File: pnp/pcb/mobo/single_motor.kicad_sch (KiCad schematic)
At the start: 8 parts, among them M2 Stepper_Motor

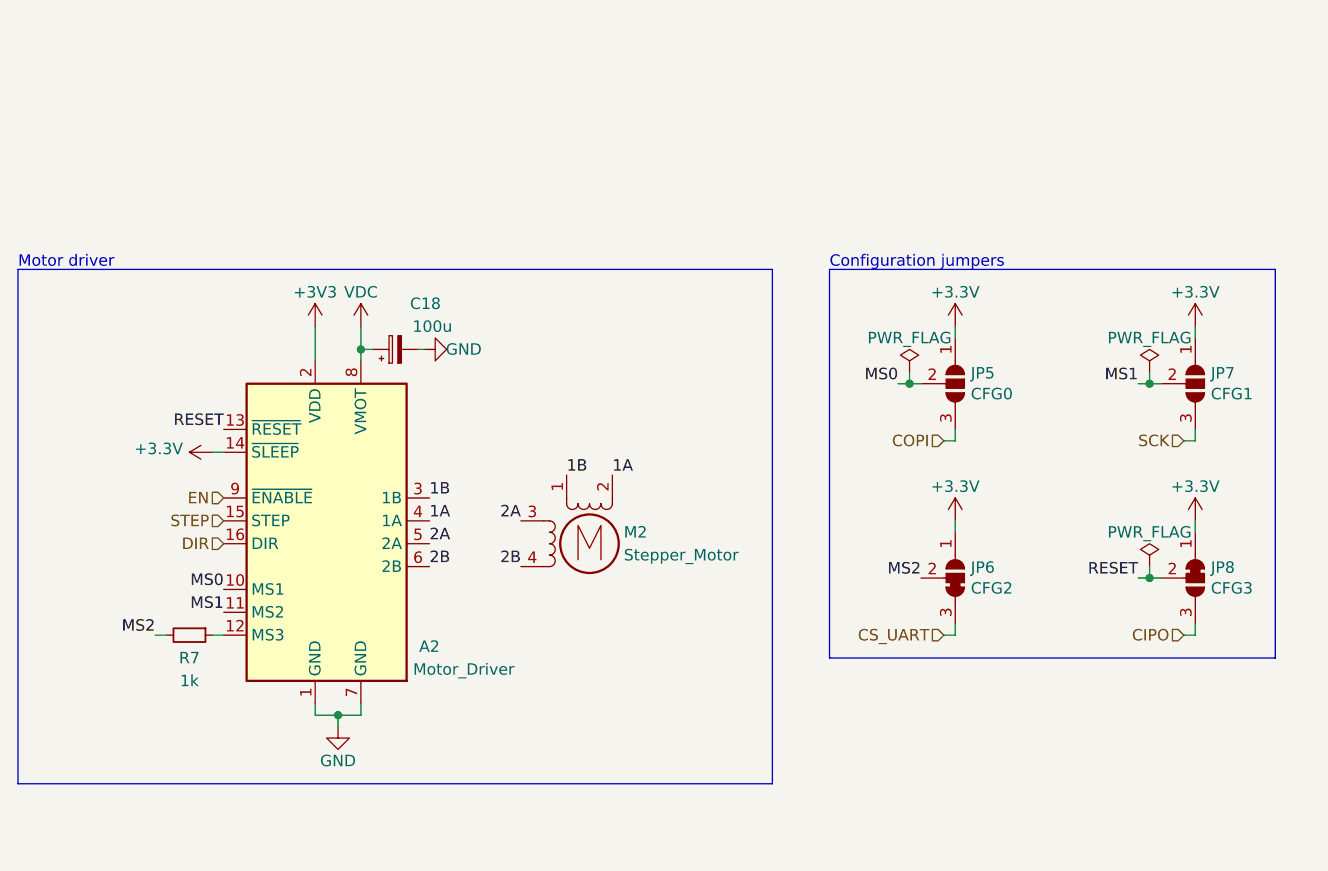
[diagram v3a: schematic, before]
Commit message: Fixed schematic parity
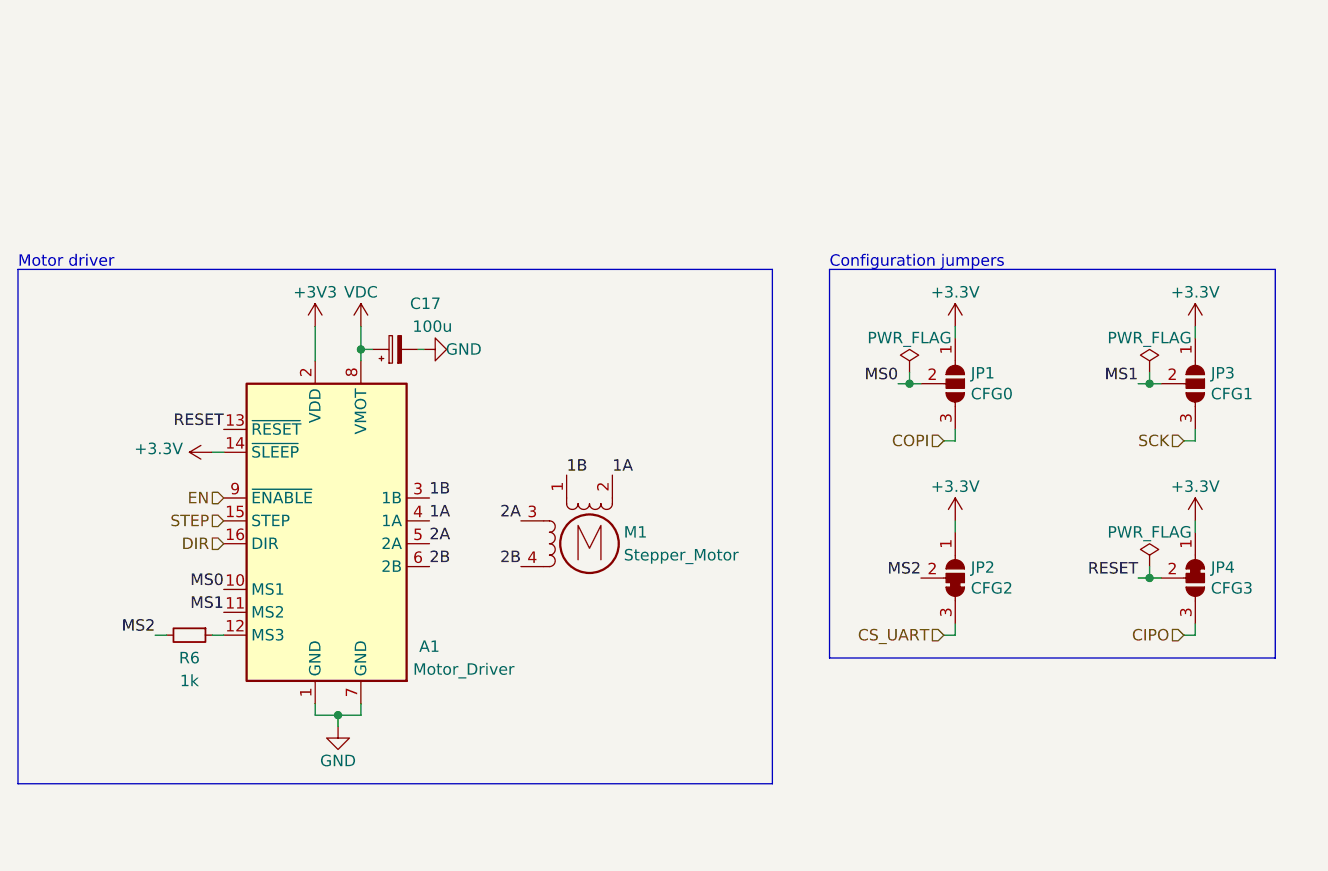
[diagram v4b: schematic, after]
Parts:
- JP2: renamed from JP6; footprint index:SolderJumper-3_P1.3mm_Bridged23_RoundedPad1.0x1.5mm -> (none)
- renumbered A2 to A1, C18 to C17, JP5 to JP1, JP7 to JP3, JP8 to JP4, M2 to M1, R7 to R6
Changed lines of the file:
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@@
     (effects (font (size 1.27 1.27)) (justify right))
   )
-  (symbol (lib_id "power:+3.3V") (at 208.28 105.41 0)
-    (in_bom yes) (on_board yes)
-    (property "Reference" "#PWR0181" (id 0) (at 208.28 109.22 0)
+  (symbol (lib_id "power:+3.3V") (at 208.28 105.41 0) (unit 1)
+    (in_bom yes) (on_board yes)
+    (property "Reference" "#PWR0142" (id 0) (at 208.28 109.22 0)
       (effects (font (size 1.27 1.27)) hide)
     )
@@
     (pin "1")
   )
-  (symbol (lib_id "power:PWR_FLAG") (at 203.2 110.49 0)
-    (in_bom yes) (on_board yes)
-    (property "Reference" "#FLG0108" (id 0) (at 203.2 108.585 0)
+  (symbol (lib_id "power:PWR_FLAG") (at 203.2 110.49 0) (unit 1)
+    (in_bom yes) (on_board yes)
+    (property "Reference" "#FLG0105" (id 0) (at 203.2 108.585 0)
       (effects (font (size 1.27 1.27)) hide)
     )
@@
     (pin "1")
   )
-  (symbol (lib_id "Device:R_Small") (at 96.52 118.11 270)
-    (in_bom yes) (on_board yes)
-    (property "Reference" "R7" (id 0) (at 96.52 120.65 90))
+  (symbol (lib_id "Device:R_Small") (at 96.52 118.11 270) (unit 1)
+    (in_bom yes) (on_board yes)
+    (property "Reference" "R6" (id 0) (at 96.52 120.65 90))
     (property "Value" "1k" (id 1) (at 96.52 123.19 90))
     (property "Footprint" "Resistor_SMD:R_0805_2012Metric" (id 2) (at 96.52 116.332 90)
@@
     (pin "2")
   )
-  (symbol (lib_id "power:+3.3V") (at 181.61 83.82 0)
-    (in_bom yes) (on_board yes)
-    (property "Reference" "#PWR0182" (id 0) (at 181.61 87.63 0)
+  (symbol (lib_id "power:+3.3V") (at 181.61 83.82 0) (unit 1)
+    (in_bom yes) (on_board yes)
+    (property "Reference" "#PWR0144" (id 0) (at 181.61 87.63 0)
       (effects (font (size 1.27 1.27)) hide)
     )
@@
     (pin "1")
   )
-  (symbol (lib_id "power:GND") (at 113.03 128.27 0)
-    (in_bom yes) (on_board yes)
-    (property "Reference" "#PWR0202" (id 0) (at 113.03 134.62 0)
+  (symbol (lib_id "power:GND") (at 113.03 128.27 0) (unit 1)
+    (in_bom yes) (on_board yes)
+    (property "Reference" "#PWR0179" (id 0) (at 113.03 134.62 0)
       (effects (font (size 1.27 1.27)) hide)
     )
@@
     (pin "1")
   )
-  (symbol (lib_id "power:+3.3V") (at 99.06 97.79 90)
-    (in_bom yes) (on_board yes)
-    (property "Reference" "#PWR0199" (id 0) (at 102.87 97.79 0)
+  (symbol (lib_id "power:+3.3V") (at 99.06 97.79 90) (unit 1)
+    (in_bom yes) (on_board yes)
+    (property "Reference" "#PWR0176" (id 0) (at 102.87 97.79 0)
       (effects (font (size 1.27 1.27)) hide)
     )
@@
     (pin "1")
   )
-  (symbol (lib_id "power:PWR_FLAG") (at 203.2 88.9 0)
-    (in_bom yes) (on_board yes)
-    (property "Reference" "#FLG0107" (id 0) (at 203.2 86.995 0)
+  (symbol (lib_id "power:PWR_FLAG") (at 203.2 88.9 0) (unit 1)
+    (in_bom yes) (on_board yes)
+    (property "Reference" "#FLG0104" (id 0) (at 203.2 86.995 0)
       (effects (font (size 1.27 1.27)) hide)
     )
@@
     (pin "1")
   )
-  (symbol (lib_id "power:+3.3V") (at 181.61 105.41 0)
-    (in_bom yes) (on_board yes)
-    (property "Reference" "#PWR0180" (id 0) (at 181.61 109.22 0)
+  (symbol (lib_id "power:+3.3V") (at 181.61 105.41 0) (unit 1)
+    (in_bom yes) (on_board yes)
+    (property "Reference" "#PWR0117" (id 0) (at 181.61 109.22 0)
       (effects (font (size 1.27 1.27)) hide)
     )
@@
     (pin "1")
   )
-  (symbol (lib_id "Driver_Motor:Pololu_Breakout_A4988") (at 110.49 105.41 0)
-    (in_bom yes) (on_board yes)
-    (property "Reference" "A2" (id 0) (at 123.19 119.38 0))
+  (symbol (lib_id "Driver_Motor:Pololu_Breakout_A4988") (at 110.49 105.41 0) (unit 1)
+    (in_bom yes) (on_board yes)
+    (property "Reference" "A1" (id 0) (at 123.19 119.38 0))
     (property "Value" "Motor_Driver" (id 1) (at 127 121.92 0))
     (property "Footprint" "Module:Pololu_Breakout-16_15.2x20.3mm" (id 2) (at 117.475 124.46 0)
@@
     (pin "9")
   )
-  (symbol (lib_id "power:GND") (at 122.555 86.36 90)
-    (in_bom yes) (on_board yes)
-    (property "Reference" "#PWR0184" (id 0) (at 128.905 86.36 0)
+  (symbol (lib_id "power:GND") (at 122.555 86.36 90) (unit 1)
+    (in_bom yes) (on_board yes)
+    (property "Reference" "#PWR0166" (id 0) (at 128.905 86.36 0)
       (effects (font (size 1.27 1.27)) hide)
     )
@@
     (pin "1")
   )
-  (symbol (lib_id "power:+3.3V") (at 208.28 83.82 0)
-    (in_bom yes) (on_board yes)
-    (property "Reference" "#PWR0183" (id 0) (at 208.28 87.63 0)
+  (symbol (lib_id "power:+3.3V") (at 208.28 83.82 0) (unit 1)
+    (in_bom yes) (on_board yes)
+    (property "Reference" "#PWR0156" (id 0) (at 208.28 87.63 0)
       (effects (font (size 1.27 1.27)) hide)
     )
@@
     (pin "1")
   )
-  (symbol (lib_id "power:VDC") (at 115.57 83.82 0)
-    (in_bom yes) (on_board yes)
-    (property "Reference" "#PWR0201" (id 0) (at 115.57 86.36 0)
+  (symbol (lib_id "power:VDC") (at 115.57 83.82 0) (unit 1)
+    (in_bom yes) (on_board yes)
+    (property "Reference" "#PWR0178" (id 0) (at 115.57 86.36 0)
       (effects (font (size 1.27 1.27)) hide)
     )
@@
     (pin "1")
   )
-  (symbol (lib_id "Device:C_Polarized_Small") (at 119.38 86.36 90)
-    (in_bom yes) (on_board yes)
-    (property "Reference" "C18" (id 0) (at 124.46 81.28 90)
+  (symbol (lib_id "Device:C_Polarized_Small") (at 119.38 86.36 90) (unit 1)
+    (in_bom yes) (on_board yes)
+    (property "Reference" "C17" (id 0) (at 124.46 81.28 90)
       (effects (font (size 1.27 1.27)) (justify left))
     )
@@
     (pin "2")
   )
-  (symbol (lib_id "Jumper:SolderJumper_3_Open") (at 181.61 90.17 270)
-    (in_bom yes) (on_board yes)
-    (property "Reference" "JP5" (id 0) (at 183.3372 89.0016 90)
+  (symbol (lib_id "Jumper:SolderJumper_3_Open") (at 181.61 90.17 270) (unit 1)
+    (in_bom yes) (on_board yes)
+    (property "Reference" "JP1" (id 0) (at 183.3372 89.0016 90)
       (effects (font (size 1.27 1.27)) (justify left))
     )
@@
     (pin "3")
   )
-  (symbol (lib_id "power:PWR_FLAG") (at 176.53 88.9 0)
-    (in_bom yes) (on_board yes)
-    (property "Reference" "#FLG0109" (id 0) (at 176.53 86.995 0)
+  (symbol (lib_id "power:PWR_FLAG") (at 176.53 88.9 0) (unit 1)
+    (in_bom yes) (on_board yes)
+    (property "Reference" "#FLG0106" (id 0) (at 176.53 86.995 0)
       (effects (font (size 1.27 1.27)) hide)
     )
@@
     (pin "1")
   )
-  (symbol (lib_id "power:+3V3") (at 110.49 83.82 0)
-    (in_bom yes) (on_board yes)
-    (property "Reference" "#PWR0200" (id 0) (at 110.49 87.63 0)
+  (symbol (lib_id "power:+3V3") (at 110.49 83.82 0) (unit 1)
+    (in_bom yes) (on_board yes)
+    (property "Reference" "#PWR0177" (id 0) (at 110.49 87.63 0)
       (effects (font (size 1.27 1.27)) hide)
     )
@@
     (pin "1")
   )
-  (symbol (lib_id "index:SolderJumper_3_Bridged23") (at 181.61 111.76 270) (mirror x)
-    (in_bom yes) (on_board yes)
-    (property "Reference" "JP6" (id 0) (at 183.3372 110.5916 90)
+  (symbol (lib_id "index:SolderJumper_3_Bridged23") (at 181.61 111.76 270) (mirror x) (unit 1)
+    (in_bom yes) (on_board yes)
+    (property "Reference" "JP2" (id 0) (at 183.3372 110.5916 90)
       (effects (font (size 1.27 1.27)) (justify left))
     )
@@
       (effects (font (size 1.27 1.27)) (justify left))
     )
-    (property "Footprint" "index:SolderJumper-3_P1.3mm_Bridged23_RoundedPad1.0x1.5mm" (id 2) (at 181.61 111.76 0)
+    (property "Footprint" "" (id 2) (at 181.61 111.76 0)
       (effects (font (size 1.27 1.27)) hide)
     )
@@
     (pin "3")
   )
-  (symbol (lib_id "Jumper:SolderJumper_3_Bridged12") (at 208.28 111.76 270)
-    (in_bom yes) (on_board yes)
-    (property "Reference" "JP8" (id 0) (at 210.0072 110.5916 90)
+  (symbol (lib_id "Jumper:SolderJumper_3_Bridged12") (at 208.28 111.76 270) (unit 1)
+    (in_bom yes) (on_board yes)
+    (property "Reference" "JP4" (id 0) (at 210.0072 110.5916 90)
       (effects (font (size 1.27 1.27)) (justify left))
     )
@@
     (pin "3")
   )
-  (symbol (lib_id "Motor:Stepper_Motor_bipolar") (at 140.97 107.95 0)
-    (in_bom yes) (on_board yes)
-    (property "Reference" "M2" (id 0) (at 144.78 106.68 0)
+  (symbol (lib_id "Motor:Stepper_Motor_bipolar") (at 140.97 107.95 0) (unit 1)
+    (in_bom yes) (on_board yes)
+    (property "Reference" "M1" (id 0) (at 144.78 106.68 0)
       (effects (font (size 1.27 1.27)) (justify left))
     )
@@
     (pin "4")
   )
-  (symbol (lib_id "Jumper:SolderJumper_3_Open") (at 208.28 90.17 270)
-    (in_bom yes) (on_board yes)
-    (property "Reference" "JP7" (id 0) (at 210.0072 89.0016 90)
-      (effects (font (size 1.27 1.27)) (justify left))
-    )
+  (symbol (lib_id "Jumper:SolderJumper_3_Open") (at 208.28 90.17 270) (unit 1)
+    (in_bom yes) (on_board yes)
+    (property "Reference" "JP3" (id 0) (at 210.0072 89.0016 90)
+      (effects (font (size 1.27 1.27)) (justify left))
+    )

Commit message: Fix symbol library
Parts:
- JP2: footprint (none) -> index:SolderJumper-3_P1.3mm_Bridged23_RoundedPad1.0x1.5mm
- JP3: footprint Jumper:SolderJumper-3_P1.3mm_Open_RoundedPad1.0x1.5mm -> (none)
- JP4: footprint Jumper:SolderJumper-3_P1.3mm_Bridged12_RoundedPad1.0x1.5mm -> (none)
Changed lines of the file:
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@@
       (effects (font (size 1.27 1.27)) (justify left))
     )
-    (property "Footprint" "" (id 2) (at 181.61 111.76 0)
+    (property "Footprint" "index:SolderJumper-3_P1.3mm_Bridged23_RoundedPad1.0x1.5mm" (id 2) (at 181.61 111.76 0)
       (effects (font (size 1.27 1.27)) hide)
     )
@@
       (effects (font (size 1.27 1.27)) (justify left))
     )
-    (property "Footprint" "Jumper:SolderJumper-3_P1.3mm_Bridged12_RoundedPad1.0x1.5mm" (id 2) (at 208.28 111.76 0)
+    (property "Footprint" "" (id 2) (at 208.28 111.76 0)
       (effects (font (size 1.27 1.27)) hide)
     )
@@
       (effects (font (size 1.27 1.27)) (justify left))
     )
-    (property "Footprint" "Jumper:SolderJumper-3_P1.3mm_Open_RoundedPad1.0x1.5mm" (id 2) (at 208.28 90.17 0)
+    (property "Footprint" "" (id 2) (at 208.28 90.17 0)
       (effects (font (size 1.27 1.27)) hide)
     )

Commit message: Refreshing CI
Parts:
- JP3: footprint (none) -> Jumper:SolderJumper-3_P1.3mm_Open_RoundedPad1.0x1.5mm
- JP4: footprint (none) -> Jumper:SolderJumper-3_P1.3mm_Bridged12_RoundedPad1.0x1.5mm
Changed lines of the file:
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@@
   (title_block
     (title "Motor")
-    (date "2021-02-19")
+    (date "2022-03-29")
     (rev "003")
   )
@@
       (effects (font (size 1.27 1.27)) (justify left))
     )
-    (property "Footprint" "" (id 2) (at 208.28 111.76 0)
+    (property "Footprint" "Jumper:SolderJumper-3_P1.3mm_Bridged12_RoundedPad1.0x1.5mm" (id 2) (at 208.28 111.76 0)
       (effects (font (size 1.27 1.27)) hide)
     )
@@
       (effects (font (size 1.27 1.27)) (justify left))
     )
-    (property "Footprint" "" (id 2) (at 208.28 90.17 0)
-      (effects (font (size 1.27 1.27)) hide)
-    )
+    (property "Footprint" "Jumper:SolderJumper-3_P1.3mm_Open_RoundedPad1.0x1.5mm" (id 2) (at 208.28 90.17 0)
+      (effects (font (size 1.27 1.27)) hide)
+    )

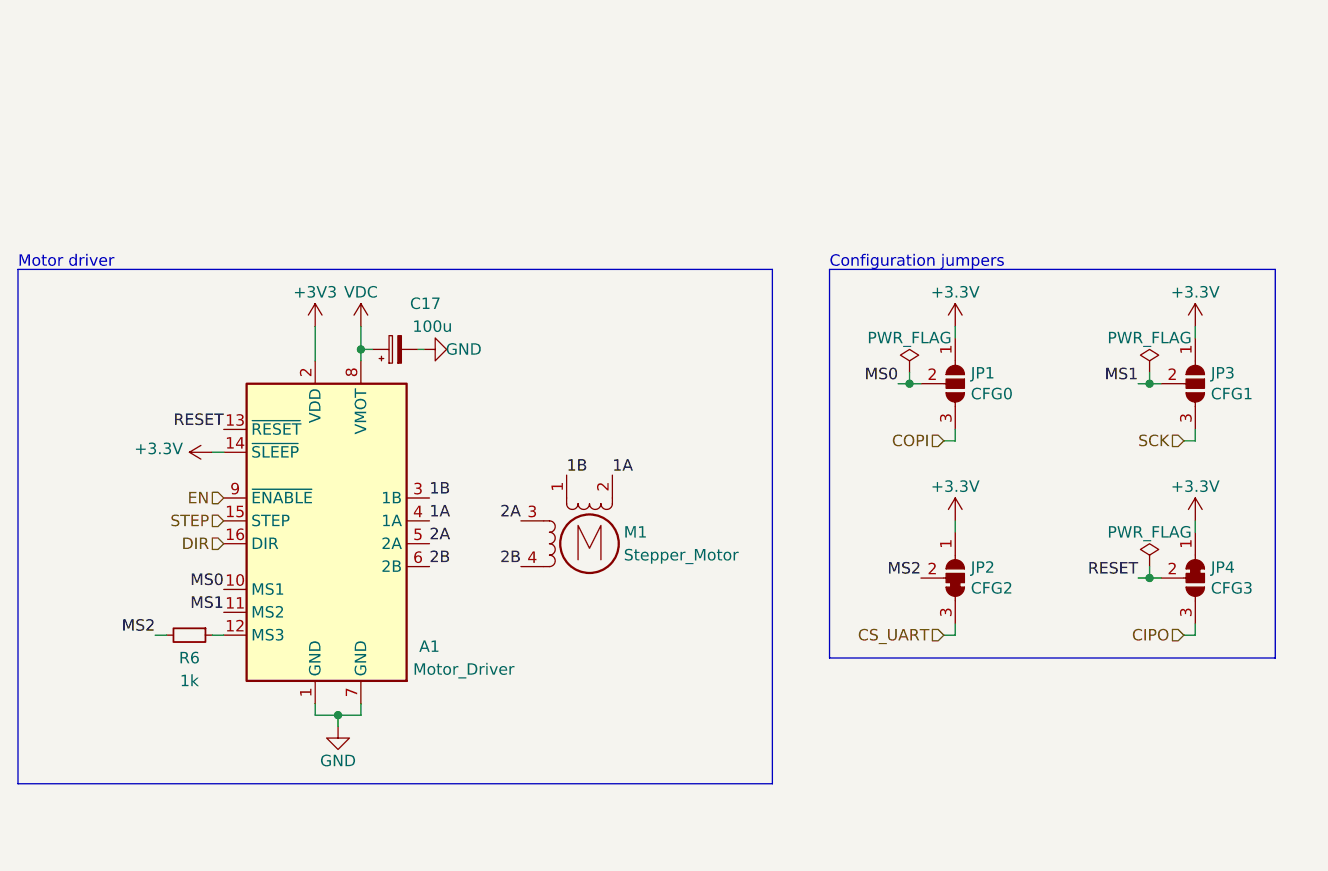
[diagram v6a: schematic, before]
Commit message: moving mobo-rev04b0 into mobo-rev04 branch from old repo
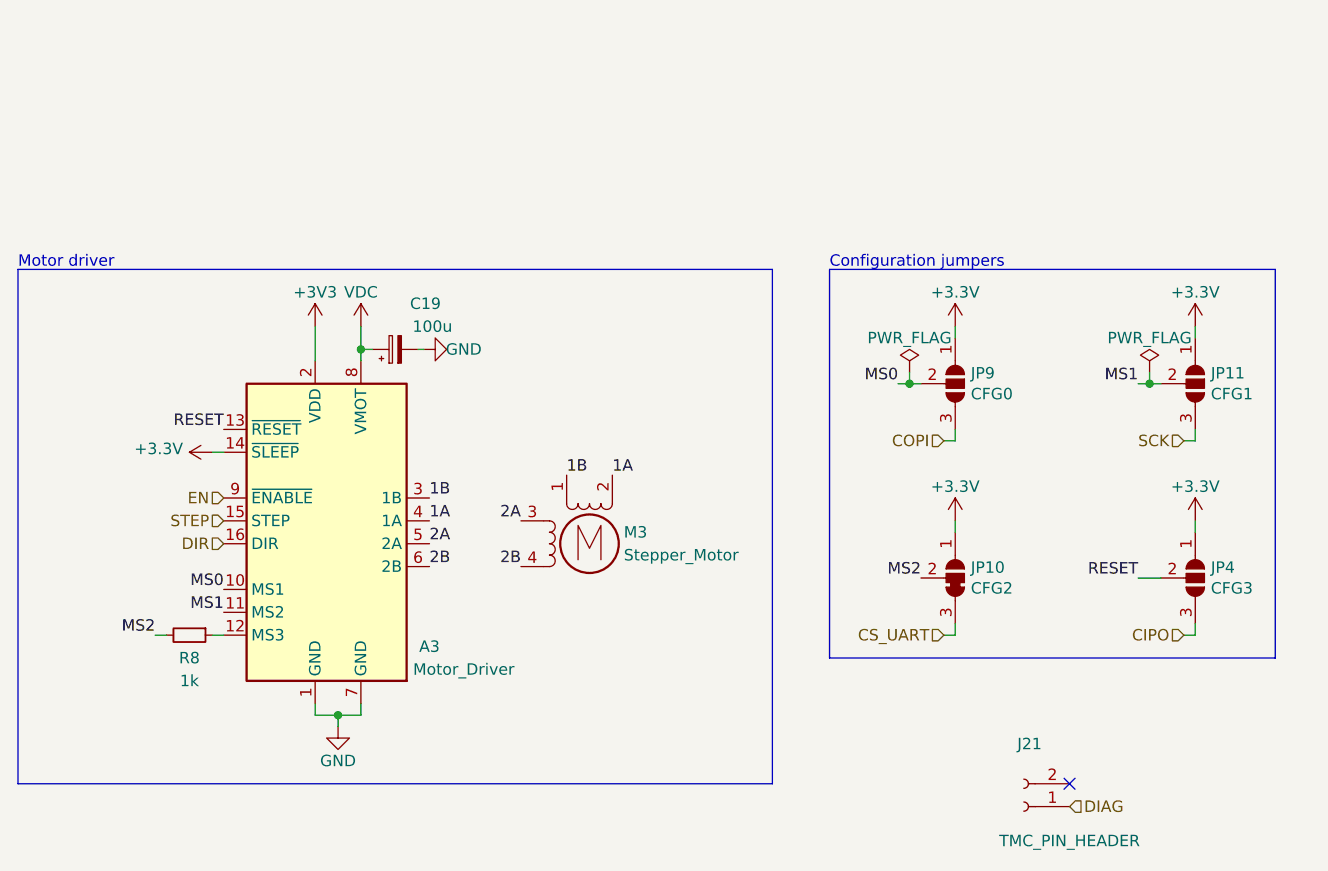
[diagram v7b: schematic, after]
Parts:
- removed JP4: CFG3, Jumper:SolderJumper-3_P1.3mm_Bridged12_RoundedPad1.0x1.5mm, symbol Jumper:SolderJumper_3_Bridged12
- added J21: TMC_PIN_HEADER, Connector_PinSocket_2.54mm:PinSocket_1x02_P2.54mm_Vertical, symbol Connector:Conn_01x02_Female
- added JP4: CFG3, Jumper:SolderJumper-3_P1.3mm_Open_RoundedPad1.0x1.5mm, symbol Jumper:SolderJumper_3_Open
- renumbered A1 to A3, C17 to C19, JP2 to JP10, JP3 to JP11, JP1 to JP9, M1 to M3, R6 to R8
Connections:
- net +3V3: now also JP4.1 (A)
- net CIPO: now also JP4.3 (B)
- net RESET: now also JP4.2 (C)
- new net DIAG: J21.1 (Pin_1)
- no-connect marks 0 -> 1
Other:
- company: (none) -> Opulo
- title: Motor -> LumenPnP Motherboard
